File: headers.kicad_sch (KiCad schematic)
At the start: 5 parts, among them J301 A2541WV-10P, J302 A2541WV-10P, J303 1715721, J304 A2541HWV-3P

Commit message: Updated schematic and board with adjustments, updated board.
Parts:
- removed J304: A2541HWV-3P, CJT Connectors:PinSocket_1x03_P2.54mm_Vertical_Female, symbol CJT Connectors:A2541HWV-3P
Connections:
- net CS renamed UPDI_C
- no-connect marks 6 -> 5
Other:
- moved on the sheet: D602, J303

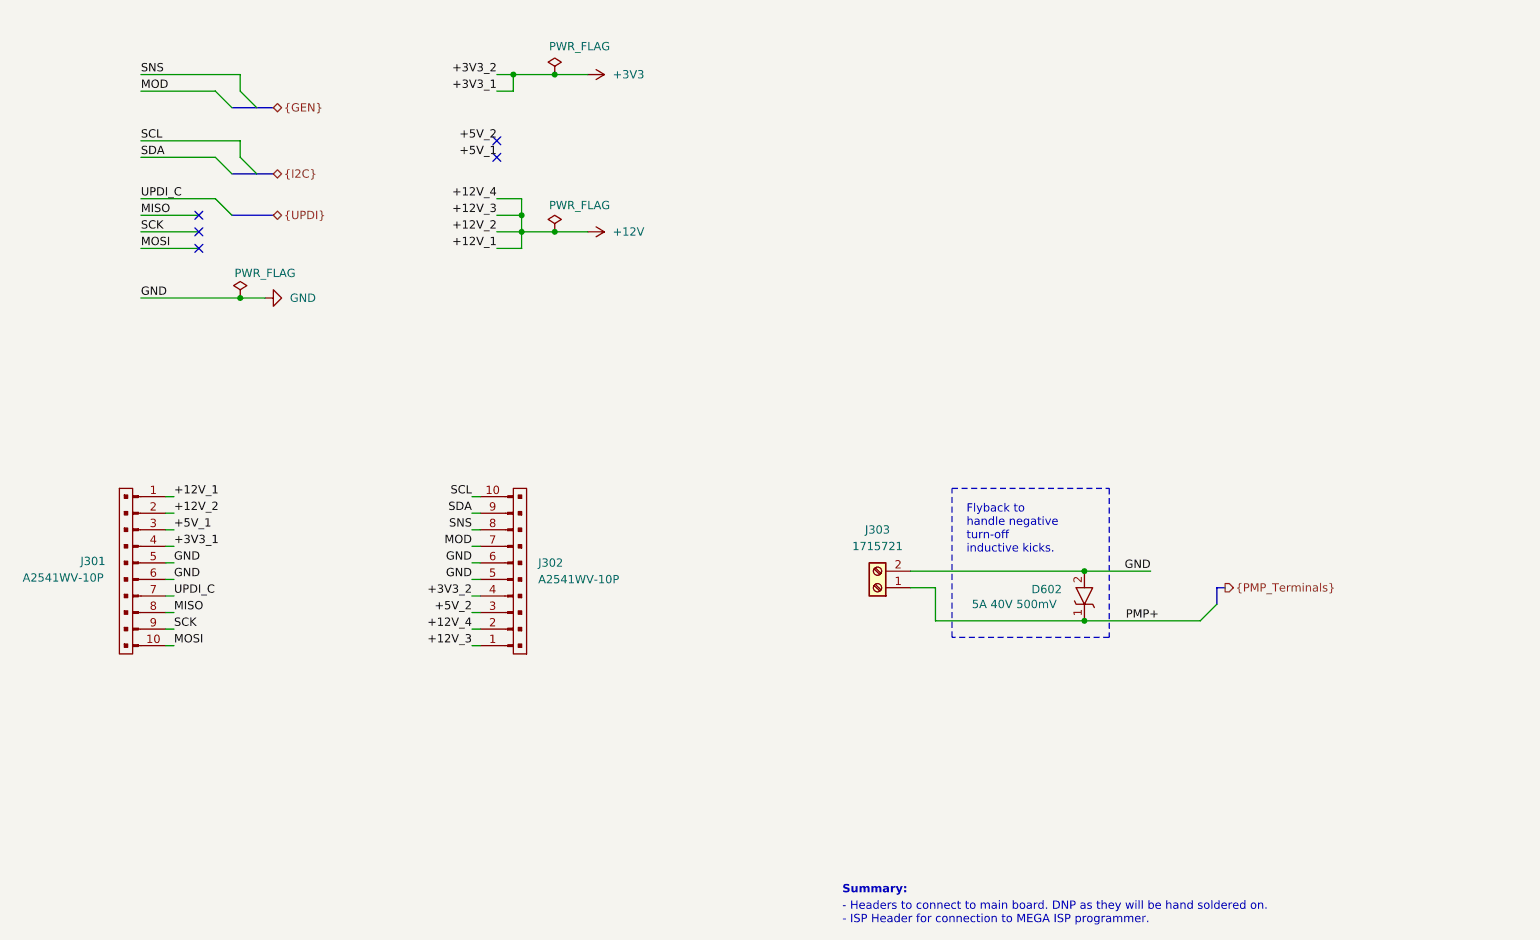
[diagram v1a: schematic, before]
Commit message: Updated schematic, redesigned and included pump pressure switch. Regenerated all outputs.
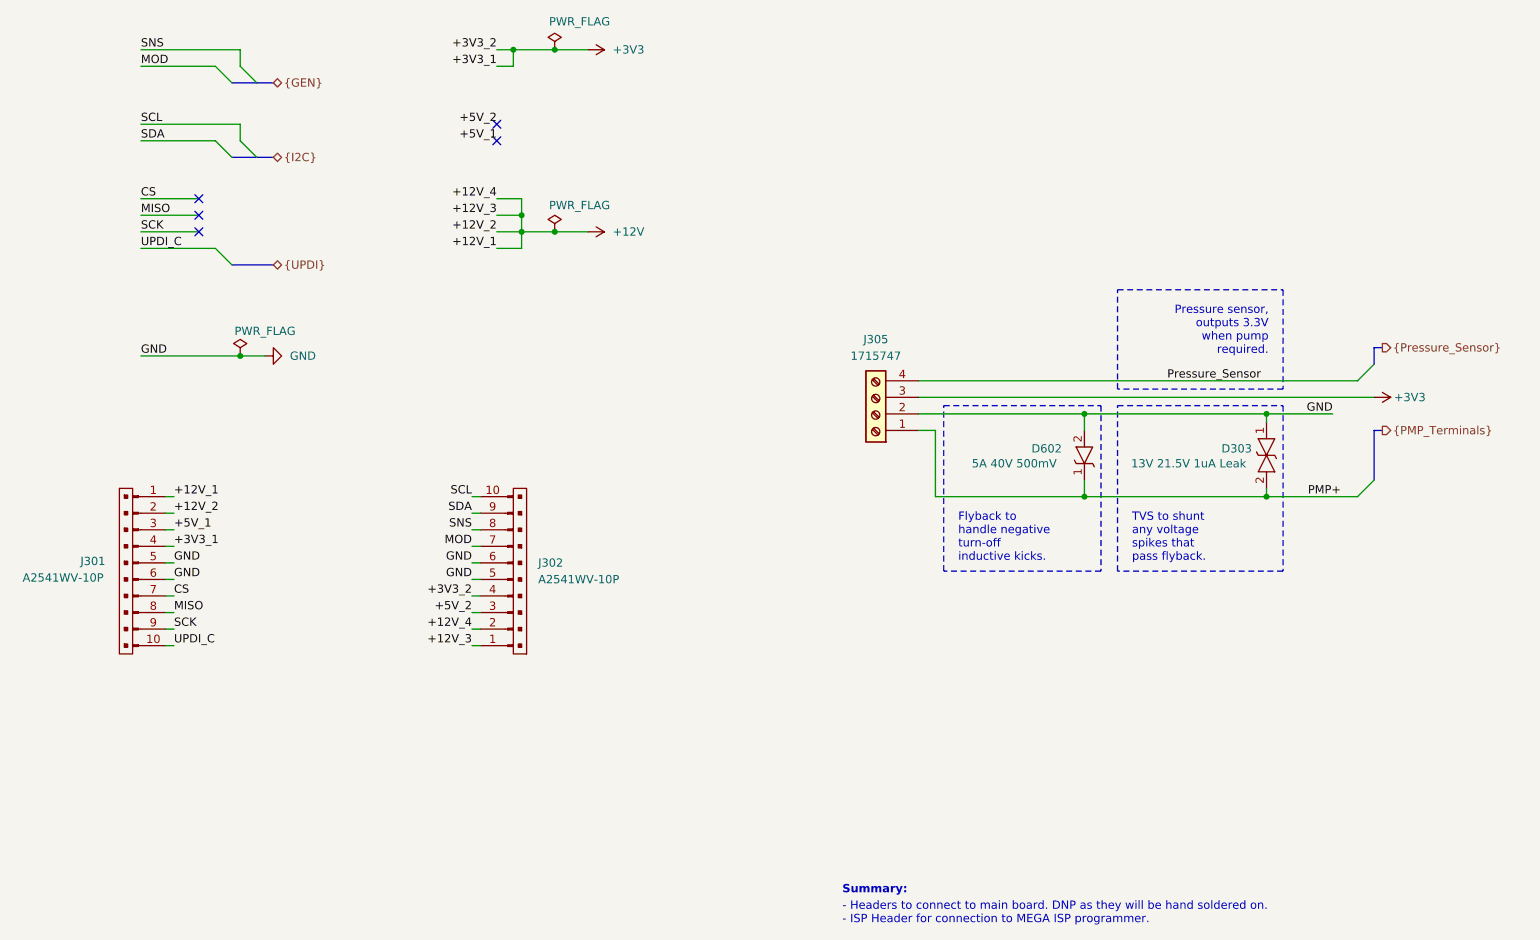
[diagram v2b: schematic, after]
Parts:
- removed J303: 1715721, PHOENIX CONTACT Terminals:1715721, symbol PHOENIX CONTACT Terminals:1715721
- added D303: 13V 21.5V 1uA Leak, LITTELFUSE Diodes:DO-214AA_Bidirectional, symbol LITTELFUSE Diodes:SMBJ13CA
- added J305: 1715747, PHOENIX CONTACT Terminals:1715747, symbol PHOENIX CONTACT Terminals:1715747
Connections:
- net MOSI is gone; now on net UPDI_C: J301.10 (Pin_10)
- net +3V3: now also J305.3
- net GND: now also D303.1 (A1), J305.2
- net PMP+: now also D303.2 (A2), J305.1
- net UPDI_C: no longer J301.7 (Pin_7)
- new net CS: J301.7 (Pin_7)
- new net Pressure_Sensor: J305.4
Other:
- moved on the sheet: D602

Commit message: Updated layout, and regenerated outputs.
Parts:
- added J303: A2541HWV-3P, CJT Connectors:PinSocket_1x03_P2.54mm_Vertical_Female, symbol CJT Connectors:A2541HWV-3P
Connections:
- net +3V3: now also J303.1 (Pin_1)
- net GND: now also J303.2 (Pin_2)
- net UPDI_C: now also J303.3 (Pin_3); no longer J301.10 (Pin_10)
- new net MOSI: J301.10 (Pin_10)
- no-connect marks 5 -> 6
